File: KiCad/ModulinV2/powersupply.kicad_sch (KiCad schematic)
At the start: 51 parts, among them IC35 NCP5500DADJR2G, IC36 NCP5500DADJR2G, IC37 LM2576S-12_NOPB, IC38 LM2576S-12_NOPB, IC39 NCP5500DADJR2G, IC40 NCP5500DADJR2G, IC41 L7812CD2T-TR, IC42 L7812CD2T-TR, J9 PJ-002B, Q3 DMP610DL-7

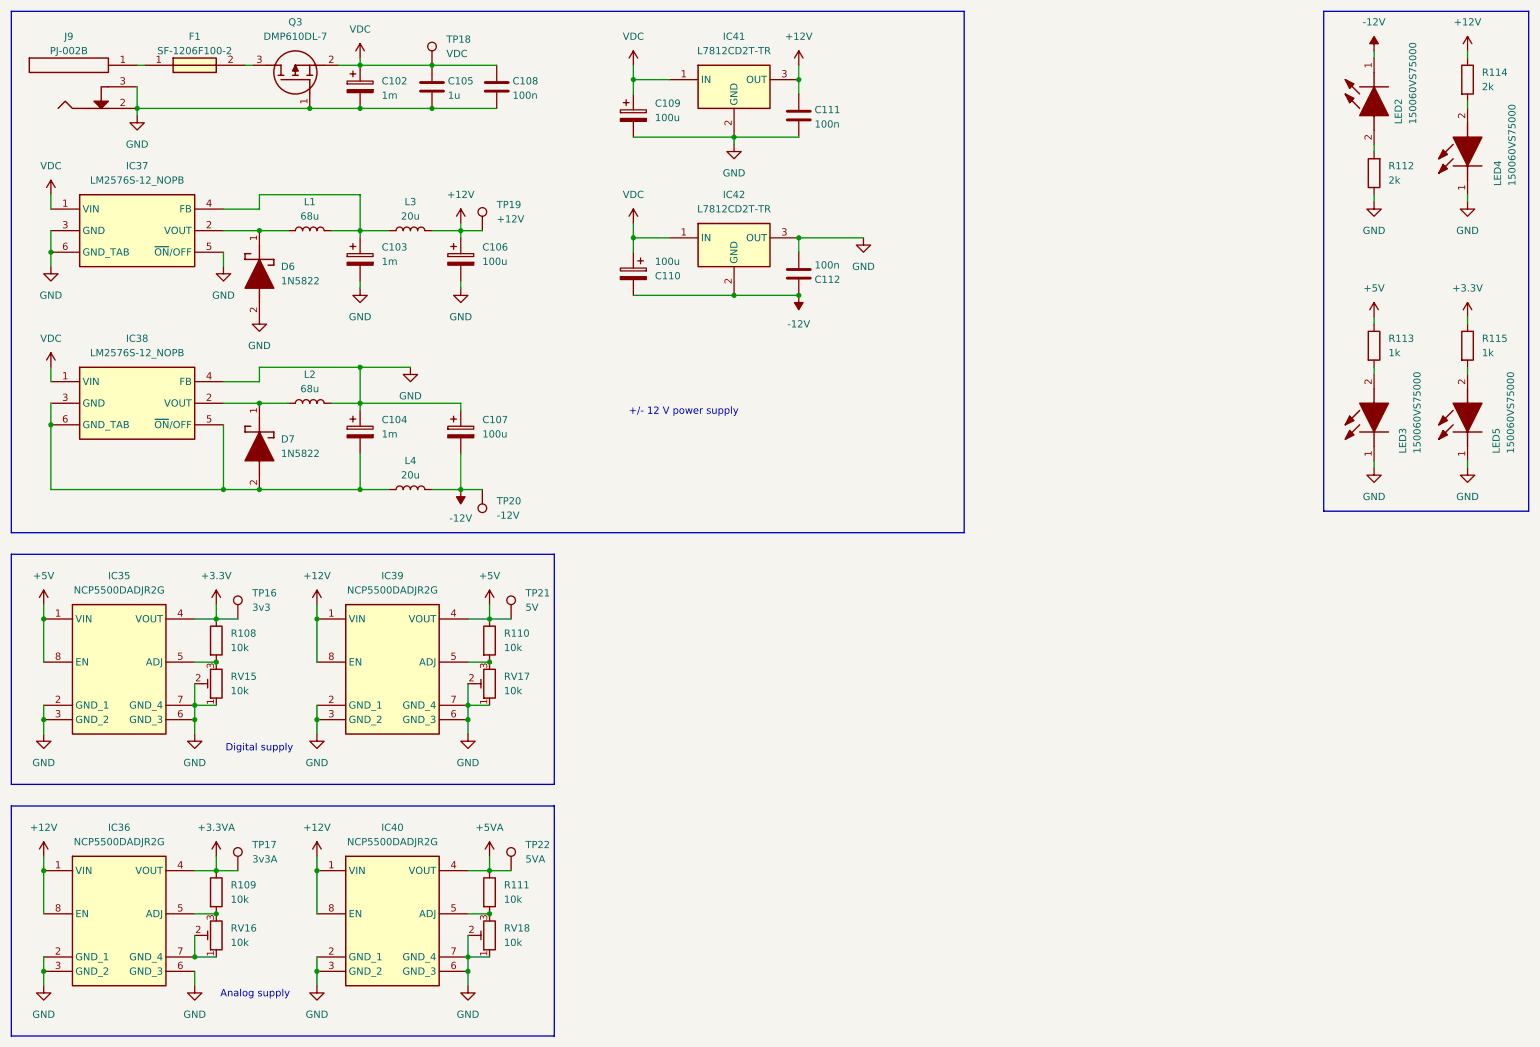
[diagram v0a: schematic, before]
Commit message: Started adding footprints for capacitors
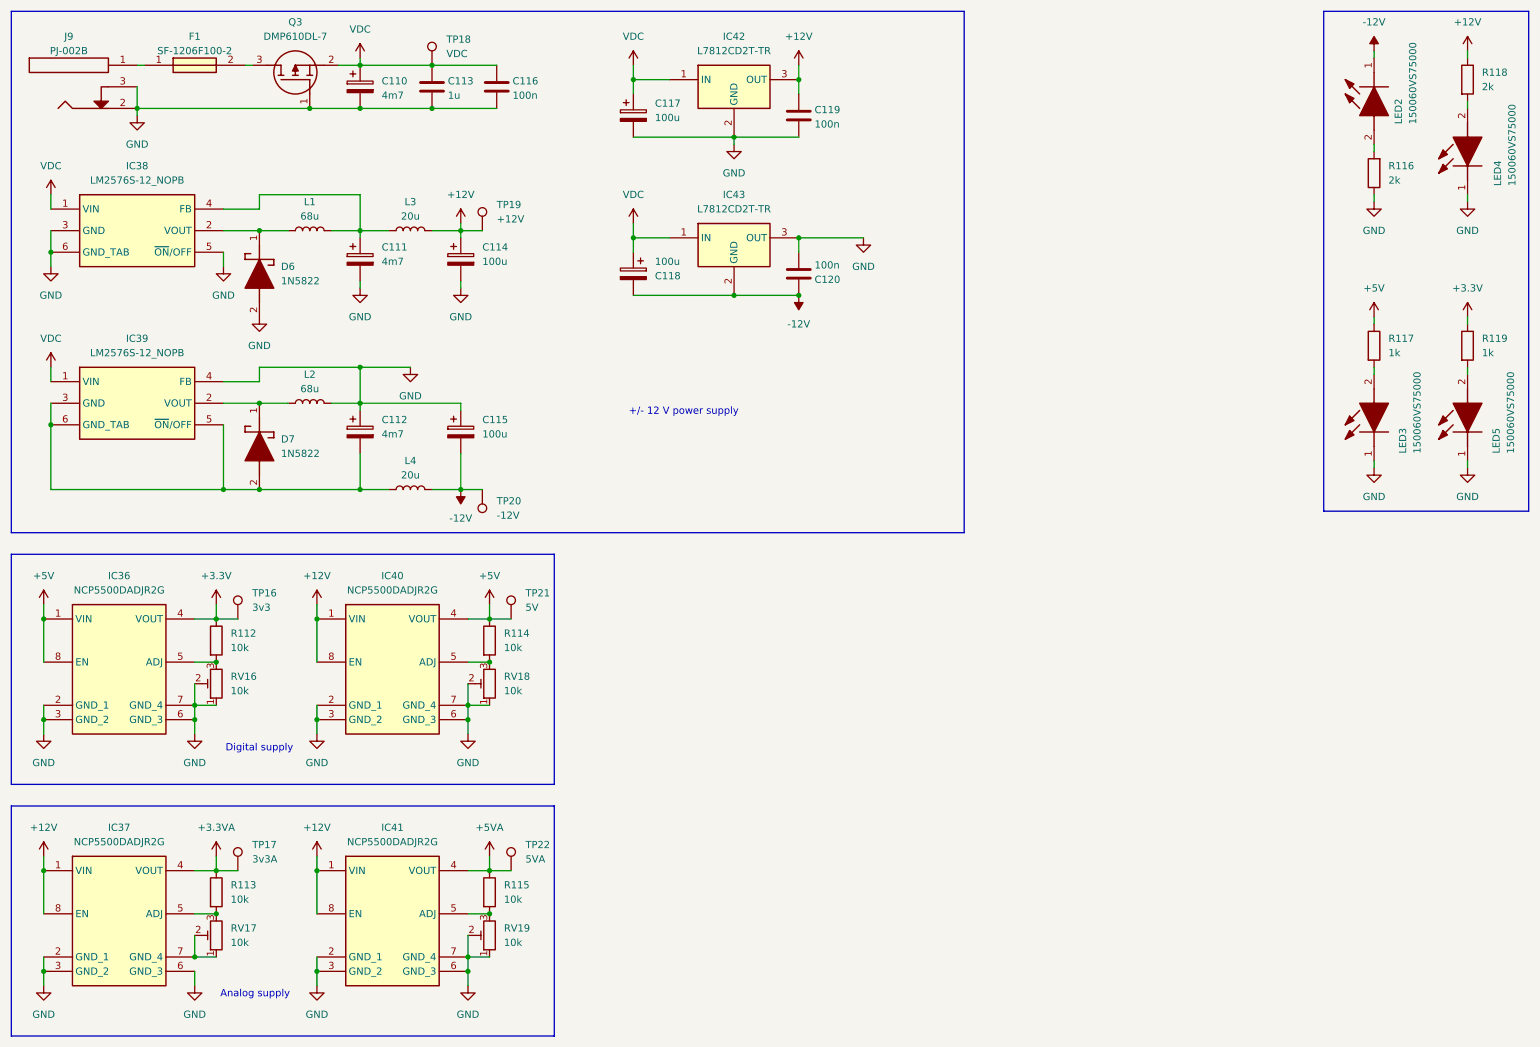
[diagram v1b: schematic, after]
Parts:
- C110: renamed from C102; value 1m -> 4m7
- C111: renamed from C103; value 1m -> 4m7
- C112: renamed from C104; value 1m -> 4m7
- C113: renamed from C105; footprint (none) -> SamacSys_Parts:CAPC1608X95N
- C116: renamed from C108; footprint (none) -> SamacSys_Parts:CAPC1608X90N
- C119: renamed from C111; footprint (none) -> SamacSys_Parts:CAPC1608X90N
- C120: renamed from C112; footprint (none) -> SamacSys_Parts:CAPC1608X90N
- L1, L2: footprint (none) -> SamacSys_Parts:VLS6045
- L3, L4: footprint (none) -> SamacSys_Parts:ETQP5M220YSC
- TP16, TP17, TP18, TP19, TP20, TP21, TP22: footprint (none) -> SamacSys_Parts:TestPointLoop
- renumbered C106 to C114, C107 to C115, C109 to C117, C110 to C118, IC35 to IC36, IC36 to IC37, IC37 to IC38, IC38 to IC39, IC39 to IC40, IC40 to IC41, IC41 to IC42, IC42 to IC43, R108 to R112, R109 to R113, R110 to R114, R111 to R115, R112 to R116, R113 to R117, R114 to R118, R115 to R119, RV15 to RV16, RV16 to RV17, RV17 to RV18, RV18 to RV19

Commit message: Added footprints to all capacitors and potentiometers
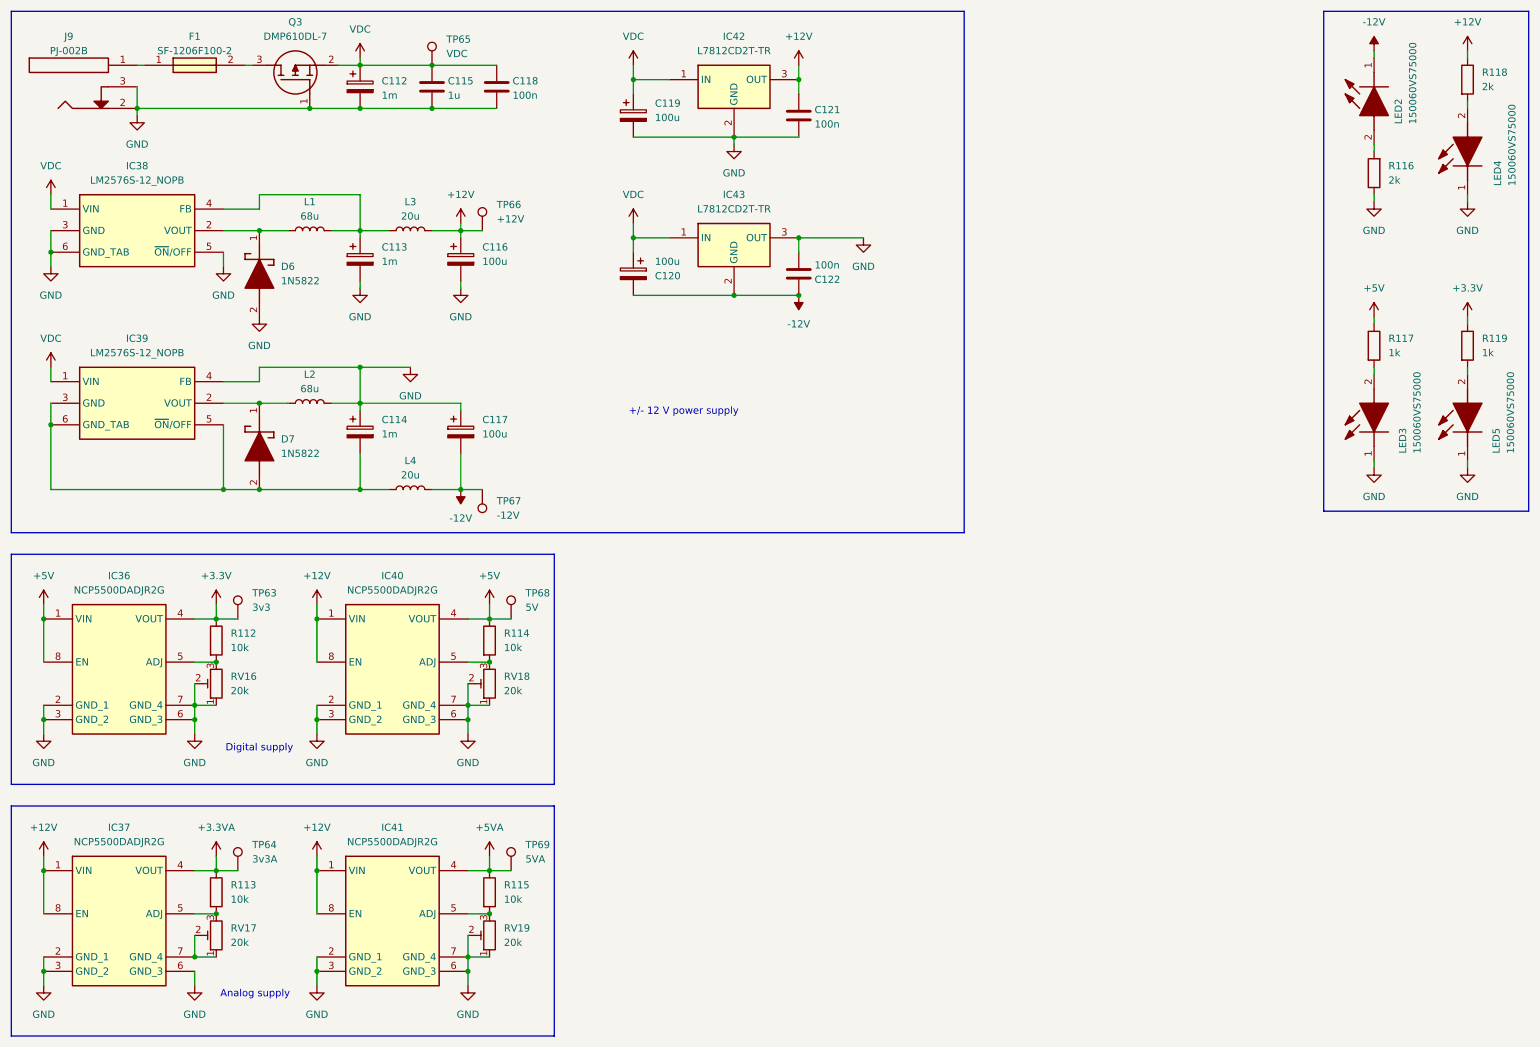
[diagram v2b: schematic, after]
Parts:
- C112: renamed from C110; value 4m7 -> 1m; footprint (none) -> SamacSys_Parts:CAPPRD500W65D1275H2700
- C113: renamed from C111; value 4m7 -> 1m; footprint (none) -> SamacSys_Parts:CAPPRD500W65D1275H2700
- C114: renamed from C112; value 4m7 -> 1m; footprint (none) -> SamacSys_Parts:CAPPRD500W65D1275H2700
- C115: renamed from C113; footprint SamacSys_Parts:CAPC1608X95N -> Capacitor_SMD:C_0603_1608Metric_Pad1.08x0.95mm_HandSolder
- C116: renamed from C114; footprint (none) -> SamacSys_Parts:ESK-_8X11_
- C117: renamed from C115; footprint (none) -> SamacSys_Parts:ESK-_8X11_
- C118: renamed from C116; footprint SamacSys_Parts:CAPC1608X90N -> Capacitor_SMD:C_0603_1608Metric_Pad1.08x0.95mm_HandSolder
- C119: renamed from C117; footprint (none) -> SamacSys_Parts:ESK-_8X11_
- C120: renamed from C118; footprint (none) -> SamacSys_Parts:ESK-_8X11_
- C121: renamed from C119; footprint SamacSys_Parts:CAPC1608X90N -> Capacitor_SMD:C_0603_1608Metric_Pad1.08x0.95mm_HandSolder
- C122: renamed from C120; footprint SamacSys_Parts:CAPC1608X90N -> Capacitor_SMD:C_0603_1608Metric_Pad1.08x0.95mm_HandSolder
- RV16, RV17, RV18, RV19: value 10k -> 20k; footprint (none) -> SamacSys_Parts:PV36W201C01B00
- renumbered TP16 to TP63, TP17 to TP64, TP18 to TP65, TP19 to TP66, TP20 to TP67, TP21 to TP68, TP22 to TP69

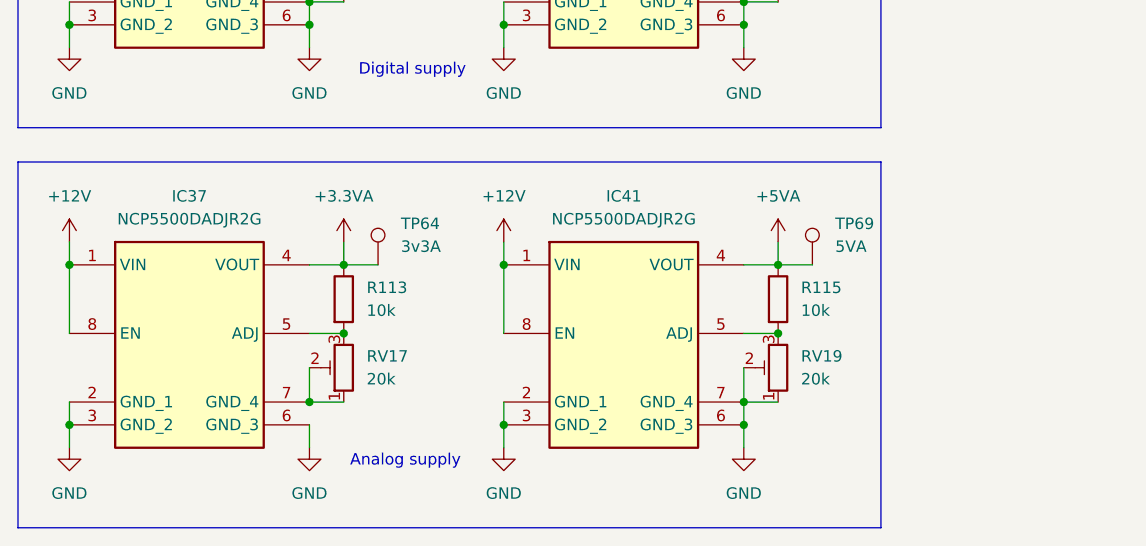
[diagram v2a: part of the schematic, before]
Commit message: Made LFO and VCF schematics in addition to making a better reference voltage supply
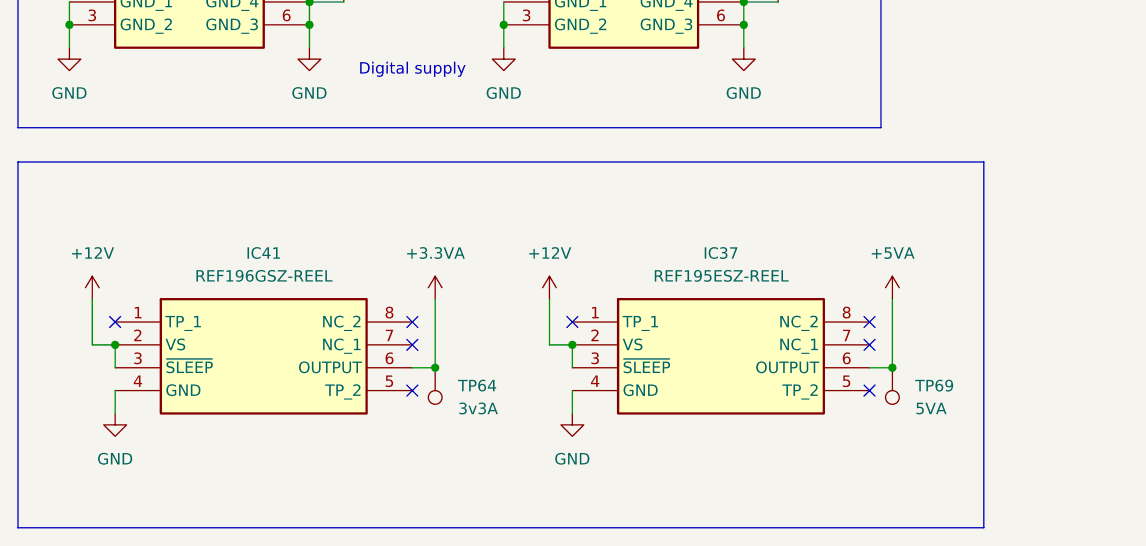
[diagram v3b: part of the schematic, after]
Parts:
- removed IC37, IC41: NCP5500DADJR2G, SamacSys_Parts:SOIC127P600X175-8N, symbol SamacSys_Parts:NCP5500DADJR2G
- removed R113, R115: 10k, symbol Device:R
- removed RV17, RV19: 20k, SamacSys_Parts:PV36W201C01B00, symbol Device:R_Potentiometer_Trim
- added IC37: REF195ESZ-REEL, SamacSys_Parts:SOIC127P600X175-8N, symbol SamacSys_Parts:REF195ESZ-REEL
- added IC41: REF196GSZ-REEL, SamacSys_Parts:SOIC127P600X175-8N, symbol SamacSys_Parts:REF196GSZ-REEL
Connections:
- net +12V: now also IC37.2 (VS), IC37.3 (~{SLEEP}), IC41.2 (VS), IC41.3 (~{SLEEP})
- net +3.3VA: now also IC41.6 (OUTPUT)
- net +5VA: now also IC37.6 (OUTPUT)
- net GND: now also IC37.4 (GND), IC41.4 (GND)
- no-connect marks 0 -> 8
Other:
- note removed: "Analog supply"
- moved on the sheet: TP64, TP69
